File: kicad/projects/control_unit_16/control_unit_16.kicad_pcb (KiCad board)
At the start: 2 copper layers, 203.2 x 97.8 mm, 54 parts, among them J1 Conn_01x04_Female, J2 Control_signal_backplane, J3 Bus_connection, J4 Aux_connection, J5 Conn_01x16_Female, U1 74HCT04, U10 28C256, U11 28C256, U2 28C256, U3 74HCT173, U4 74HCT377, U5 74HCT161, U6 28C256, U7 74HCT245, U8 74HCT245, U9 74HCT138

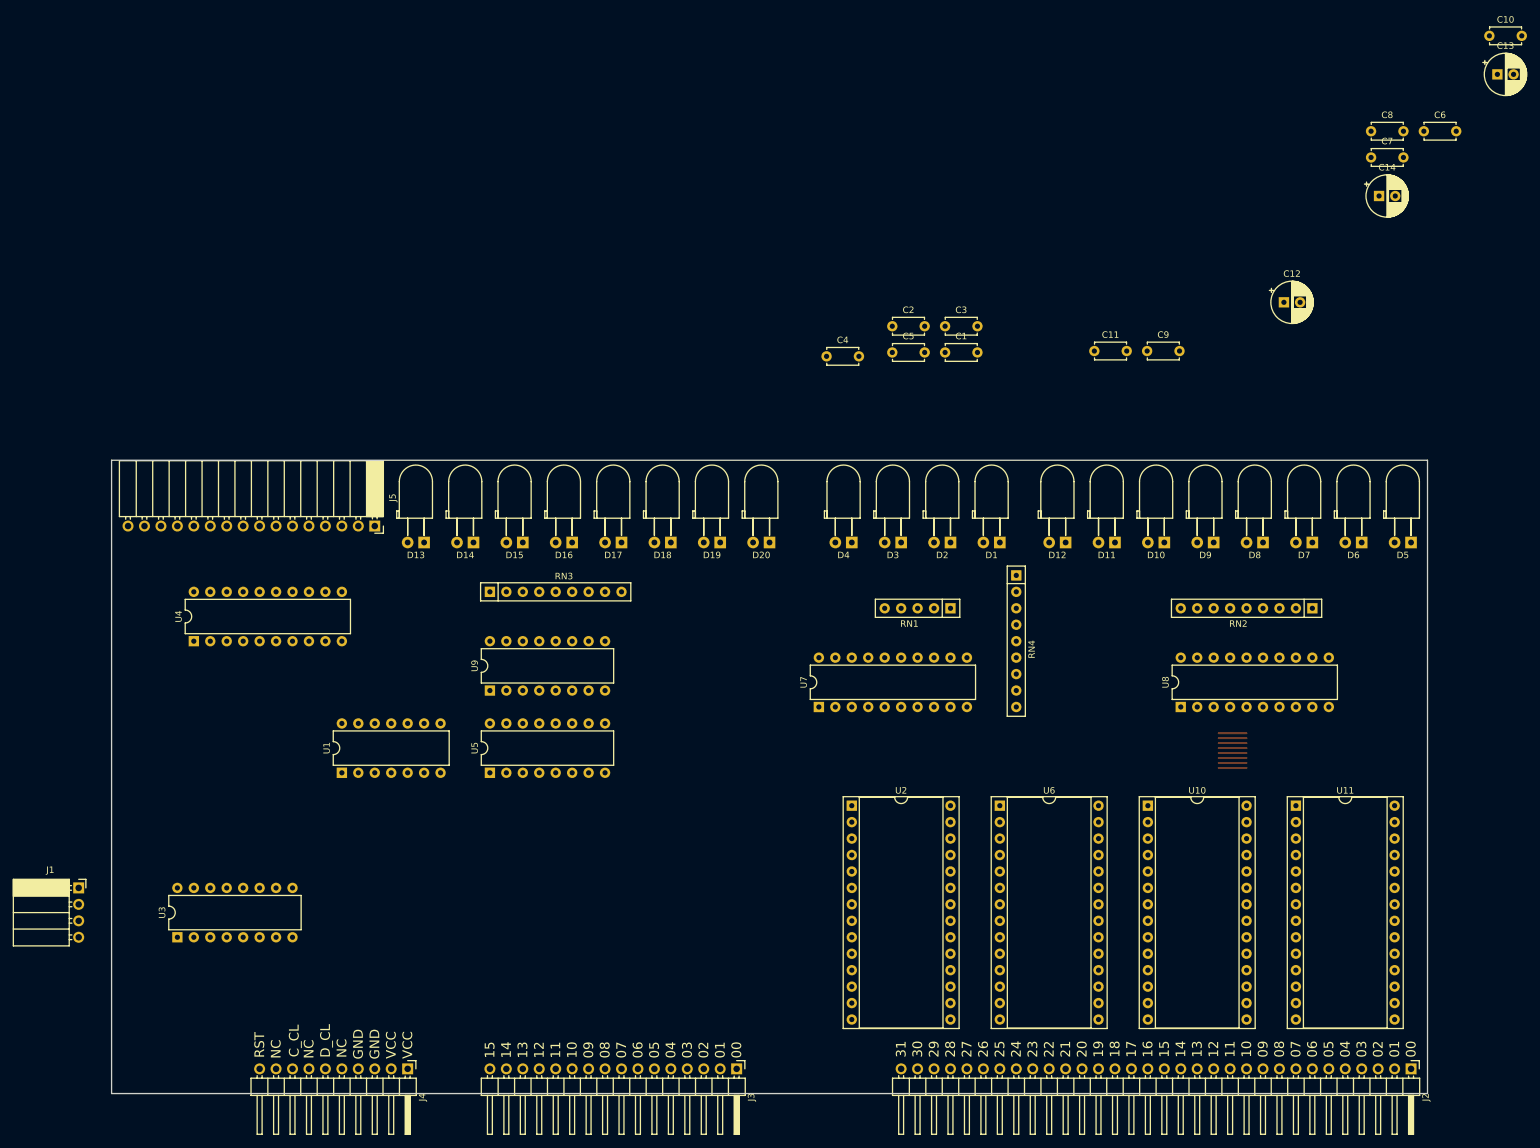
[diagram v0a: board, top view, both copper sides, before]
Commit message: About half way through control unit PCB layout.
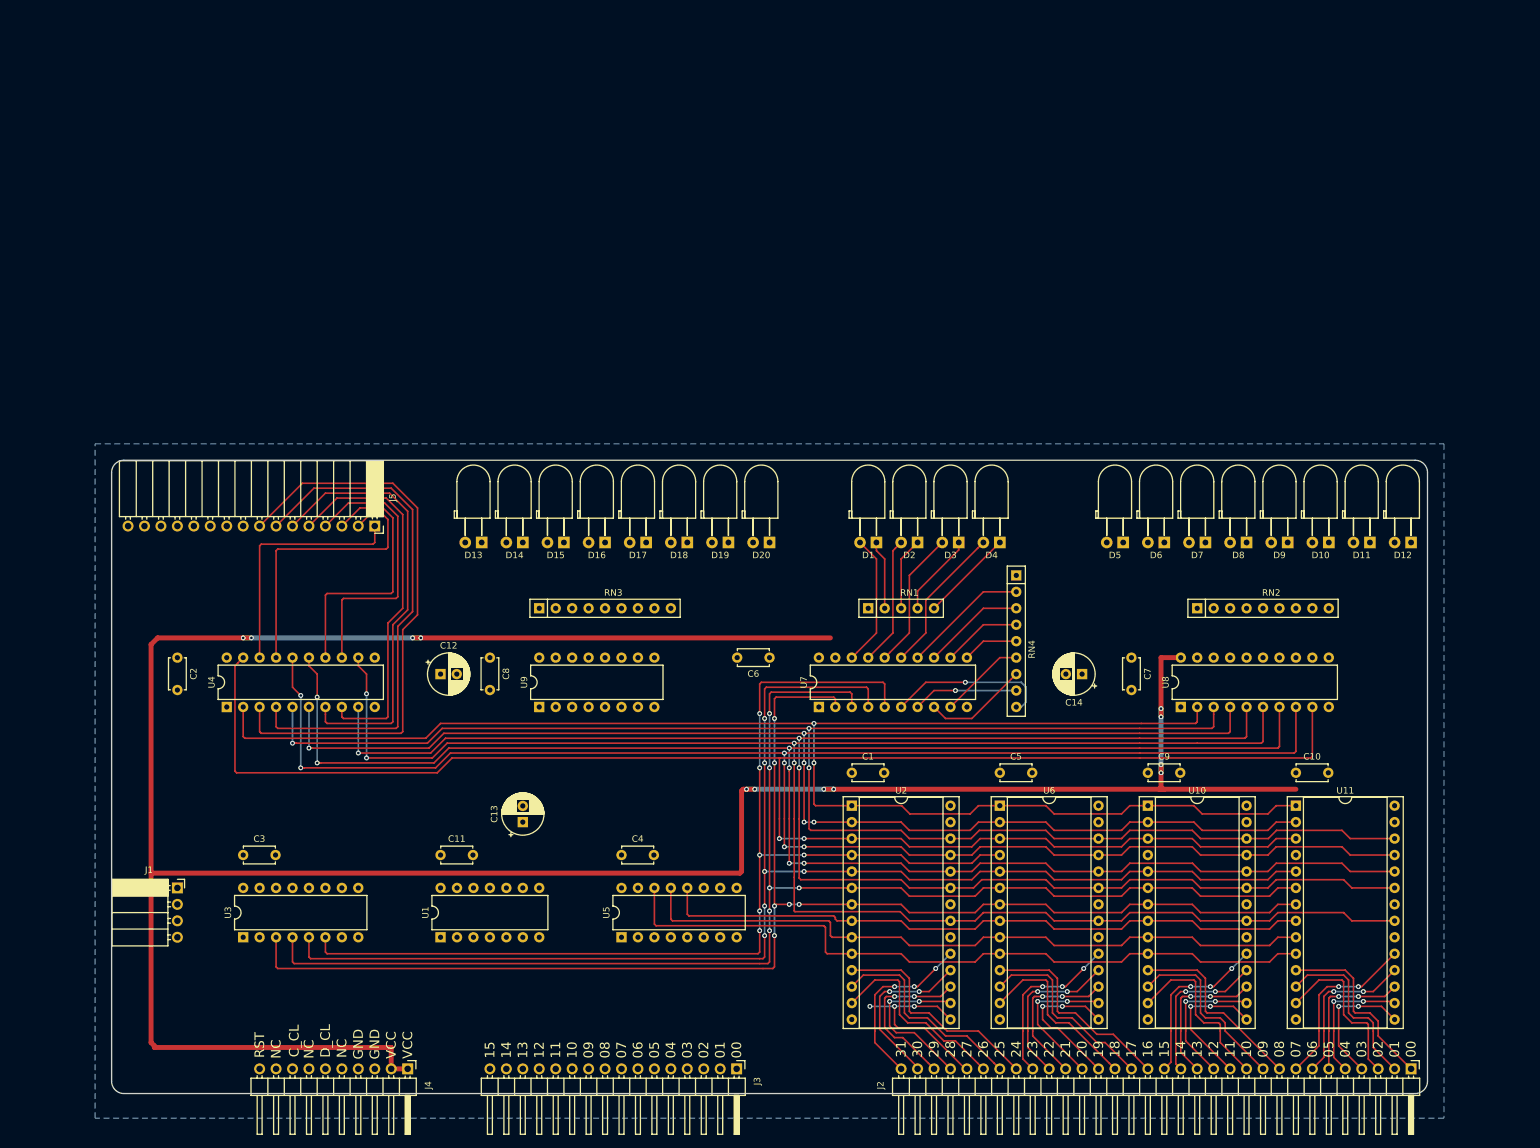
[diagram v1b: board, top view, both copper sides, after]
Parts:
- moved C13 189.7 mm to (114.3, 106.7), turned to 90 degrees
- moved C8 158.5 mm to (109.2, 81.3), turned to 270 degrees
- moved C12 142.3 mm to (101.6, 83.8)
- moved C3 135.7 mm to (71.1, 111.8)
- moved C6 129.7 mm to (152.4, 81.3), turned to 180 degrees
- moved C11 127.5 mm to (101.6, 111.8)
- moved C2 121.7 mm to (61.0, 81.3), turned to 270 degrees
- moved C10 117.7 mm to (233.7, 99.1)
- moved C14 86.9 mm to (200.7, 83.8), turned to 180 degrees
- moved C7 85.6 mm to (208.3, 81.3), turned to 270 degrees
- moved C4 83.3 mm to (129.5, 111.8)
- moved C5 67.0 mm to (188.0, 99.1)
- moved C1 66.5 mm to (165.1, 99.1)
- moved C9 65.1 mm to (210.8, 99.1)
- moved D12 53.3 mm to (251.5, 63.5)
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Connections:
- U4 pad 12: /MIR_INST_4 -> /MIR_INST_3
- U4 pad 13: /INST_04 -> /INST_03
- U4 pad 14: /INST_05 -> /INST_02
- U4 pad 15: /MIR_INST_5 -> /MIR_INST_2
- U4 pad 16: /MIR_INST_6 -> /MIR_INST_1
- U4 pad 17: /INST_06 -> /INST_01
- U4 pad 18: /INST_07 -> /INST_00
- U4 pad 19: /MIR_INST_7 -> /MIR_INST_0
- U4 pad 2: /MIR_INST_0 -> /MIR_INST_7
- U4 pad 3: /INST_00 -> /INST_07
- U4 pad 4: /INST_01 -> /INST_06
- U4 pad 5: /MIR_INST_1 -> /MIR_INST_6
- U4 pad 6: /MIR_INST_2 -> /MIR_INST_5
- U4 pad 7: /INST_02 -> /INST_05
- U4 pad 8: /INST_03 -> /INST_04
- U4 pad 9: /MIR_INST_3 -> /MIR_INST_4
- U8 pad 2: /MIR_INST_0 -> /MIR_INST_7
- U8 pad 3: /MIR_INST_1 -> /MIR_INST_6
- U8 pad 4: /MIR_INST_2 -> /MIR_INST_5
- U8 pad 5: /MIR_INST_3 -> /MIR_INST_4
- U8 pad 6: /MIR_INST_4 -> /MIR_INST_3
- U8 pad 7: /MIR_INST_5 -> /MIR_INST_2
- U8 pad 8: /MIR_INST_6 -> /MIR_INST_1
- U8 pad 9: /MIR_INST_7 -> /MIR_INST_0
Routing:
- net VCC: track 0.00 -> 433.0 mm, vias 0 -> 12
- net /MIR_INST_1: track 0.00 -> 291.8 mm, vias 0 -> 6
- net /MIR_INST_0: track 0.00 -> 288.3 mm, vias 0 -> 2
- net /MIR_INST_2: track 0.00 -> 287.5 mm, vias 0 -> 6
- net /MIR_INST_3: track 0.00 -> 283.0 mm, vias 0 -> 4
- net /MIR_INST_4: track 0.00 -> 267.2 mm, vias 0 -> 3
- net /MIR_INST_6: track 0.00 -> 261.6 mm, vias 0 -> 3
- net /MIR_INST_5: track 0.00 -> 246.3 mm, vias 0 -> 5
- net /MIR_INST_7: track 0.00 -> 245.5 mm, vias 0 -> 2
- net /MIR_NEGATIVE: track 0.00 -> 219.2 mm, vias 0 -> 6
- net /MIR_CARRY: track 0.00 -> 218.5 mm, vias 0 -> 6
- net /MIR_EQUAL: track 0.00 -> 217.8 mm, vias 0 -> 6
- net /MIR_ZERO: track 0.00 -> 172.2 mm, vias 0 -> 6
- net /BIN_STEP_0: track 0.00 -> 111.9 mm
- net /BIN_STEP_1: track 0.00 -> 106.8 mm
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- added copper zone on B.Cu, net GND
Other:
- outline, holes or cut-outs redrawn

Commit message: PCB layout done pending final checks
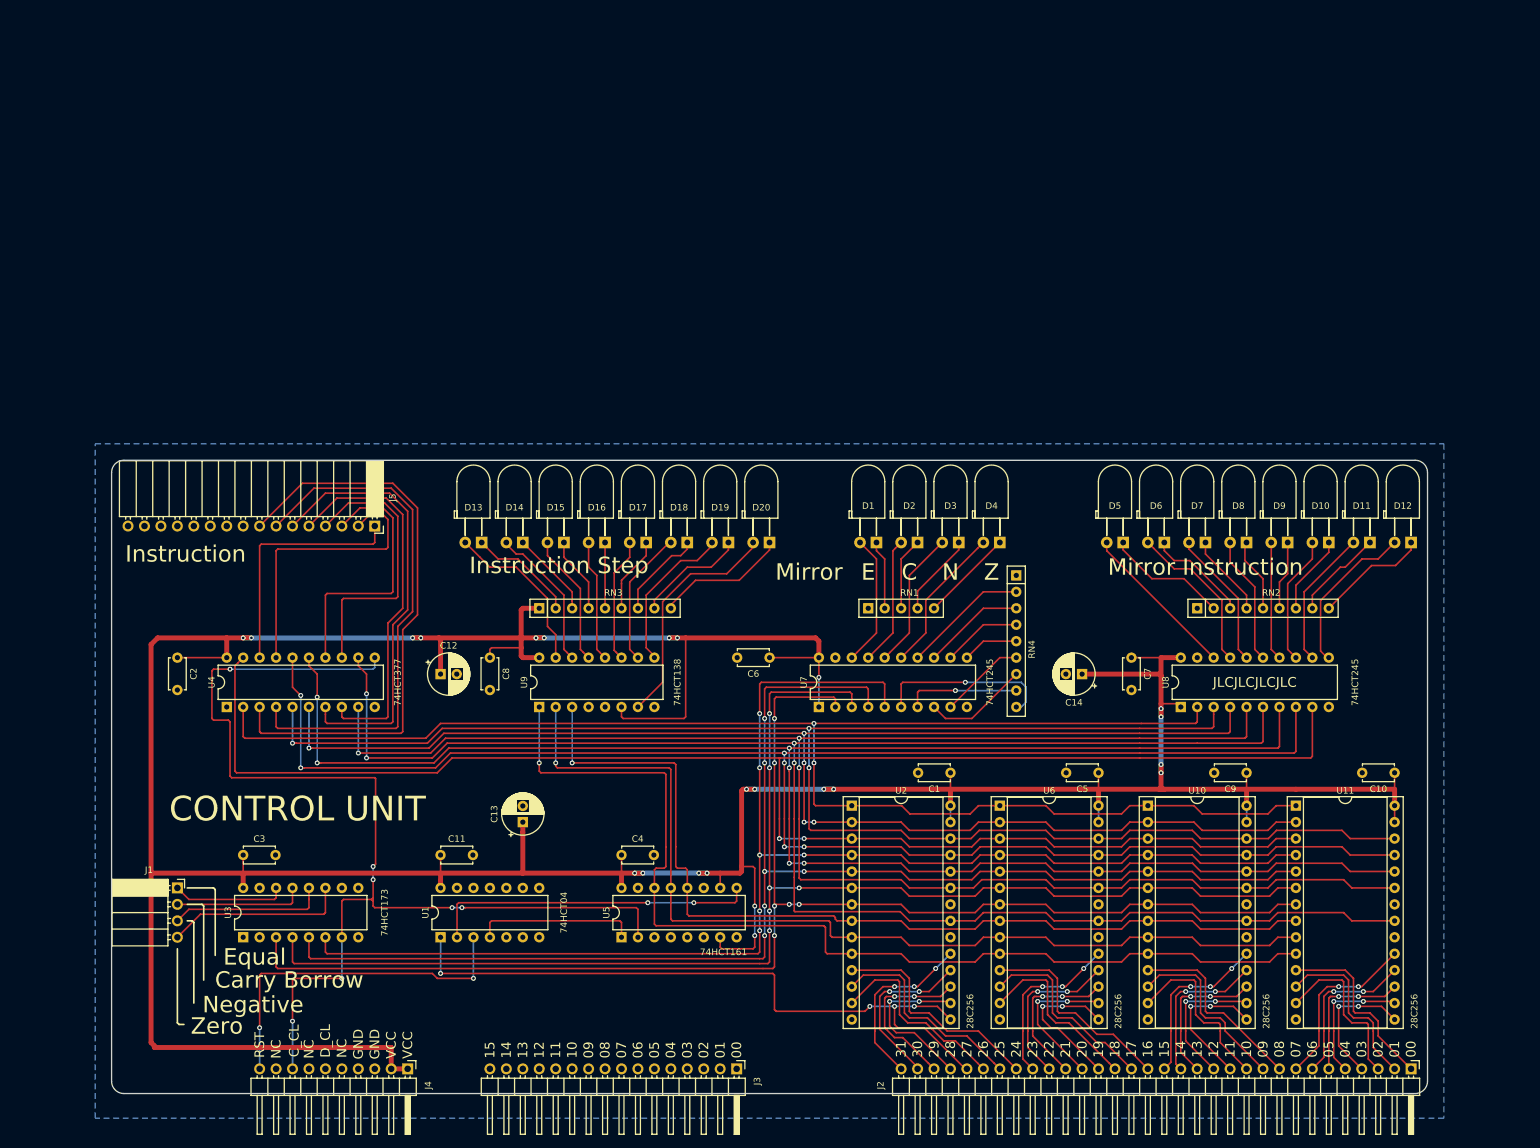
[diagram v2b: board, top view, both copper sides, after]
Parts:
- moved C1 15.2 mm to (180.3, 99.1), turned to 180 degrees
- moved C9 15.2 mm to (226.1, 99.1), turned to 180 degrees
- moved C10 15.2 mm to (248.9, 99.1), turned to 180 degrees
- moved C5 15.2 mm to (203.2, 99.1), turned to 180 degrees
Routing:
- net VCC: track 433.0 -> 626.3 mm, vias 12 -> 23
- net /CONTROL_CLOCK: track 0.00 -> 172.3 mm, vias 0 -> 7
- net /STEP_RESET: track 30.1 -> 107.8 mm, vias 3 -> 4
- net /RESET: track 0.00 -> 54.3 mm, vias 0 -> 2
- net /~STEP_RESET: track 0.00 -> 50.5 mm, vias 0 -> 2
- net /BIN_STEP_0: track 111.9 -> 160.6 mm, vias 0 -> 1
- net /MIR_ZERO: track 172.2 -> 220.0 mm
- net /BIN_STEP_1: track 106.8 -> 152.3 mm, vias 0 -> 1
- net /BIN_STEP_2: track 101.8 -> 147.0 mm, vias 0 -> 1
- net /LIN_STEP_7: track 0.00 -> 36.0 mm
- net /ZERO: track 0.00 -> 28.2 mm
- net /LIN_STEP_0: track 0.00 -> 25.9 mm
- net /~RESET: track 0.00 -> 25.1 mm
- net Net-(D12-Pad2): track 0.00 -> 24.6 mm
- net Net-(D5-Pad2): track 0.00 -> 24.6 mm
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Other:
- board text added: "C"
- board text added: "CONTROL UNIT"
- board text added: "Carry Borrow"
- board text added: "E"
- board text added: "Equal"
- board text added: "Instruction"
- board text added: "Instruction Step"
- board text added: "JLCJLCJLCJLC"
- board text added: "Mirror"
- board text added: "Mirror Instruction"
- board text added: "N"
- board text added: "Negative"
- board text added: "Z"
- board text added: "Zero"

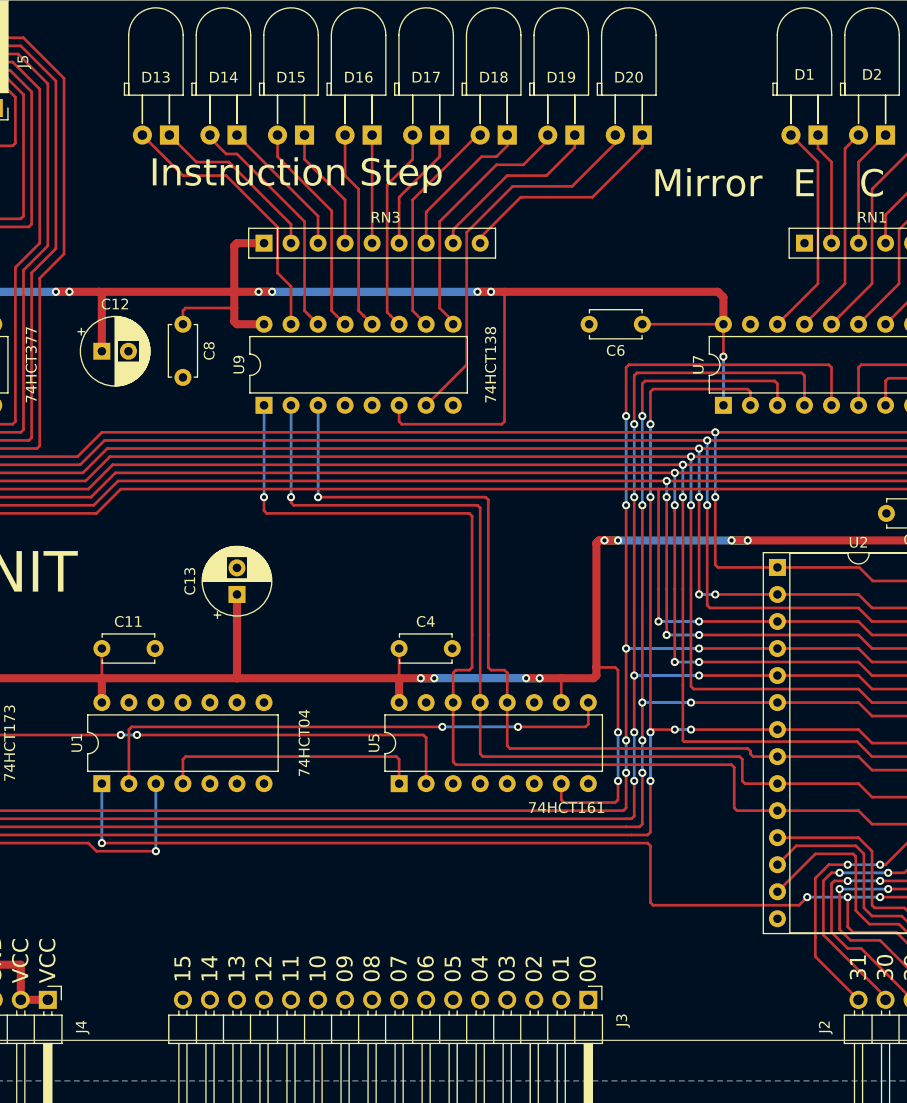
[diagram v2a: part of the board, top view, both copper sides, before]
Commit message: Move kikad libs to sixteen bit location and update projects.
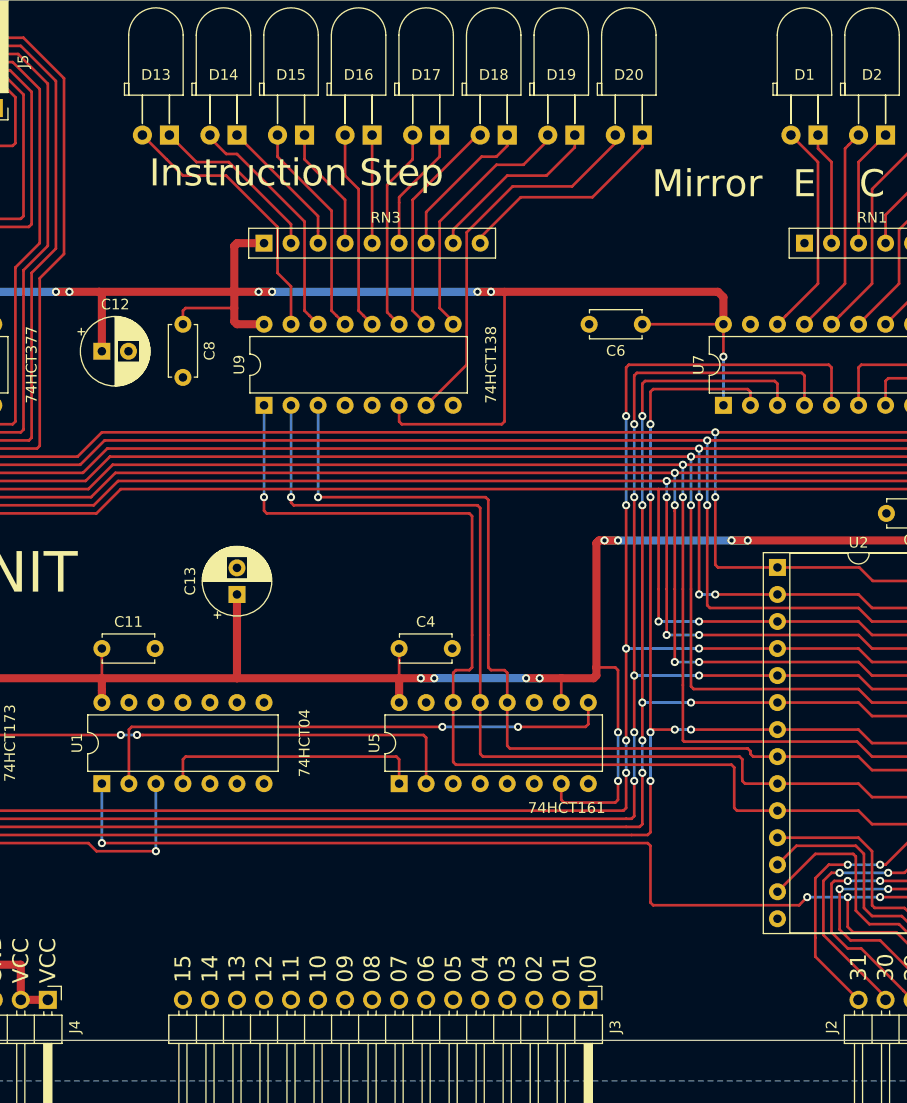
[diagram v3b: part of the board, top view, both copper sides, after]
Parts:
- D1, D10, D11, D12, D13, D14, D15, D16, D17, D18, D19, D2, D20, D3, D4, D5, D6, D7, D8, D9: footprint eight-bit-computer:LED_D5.0mm_Horizontal_O3.81mm_Z3.0mm -> sixteen-bit-computer:LED_D5.0mm_Horizontal_O3.81mm_Z3.0mm
- J2: footprint eight-bit-computer:backplane-connector-single-row -> sixteen-bit-computer:backplane-connector-single-row
- J3: footprint eight-bit-computer:bus-connection -> sixteen-bit-computer:bus-connection
- J4: footprint eight-bit-computer:aux-connection -> sixteen-bit-computer:aux-connection
